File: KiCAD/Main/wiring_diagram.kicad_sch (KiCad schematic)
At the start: 20 parts, among them J5 Screw_Terminal_01x09, J6 Screw_Terminal_01x09, M1 Motor_Servo [Axon Mini MkII], M2 Motor_Servo [Axon Mini MkII], SW3 Screw Switch, SW4 Screw Switch, SW5 Screw Switch, SW6 Screw Switch

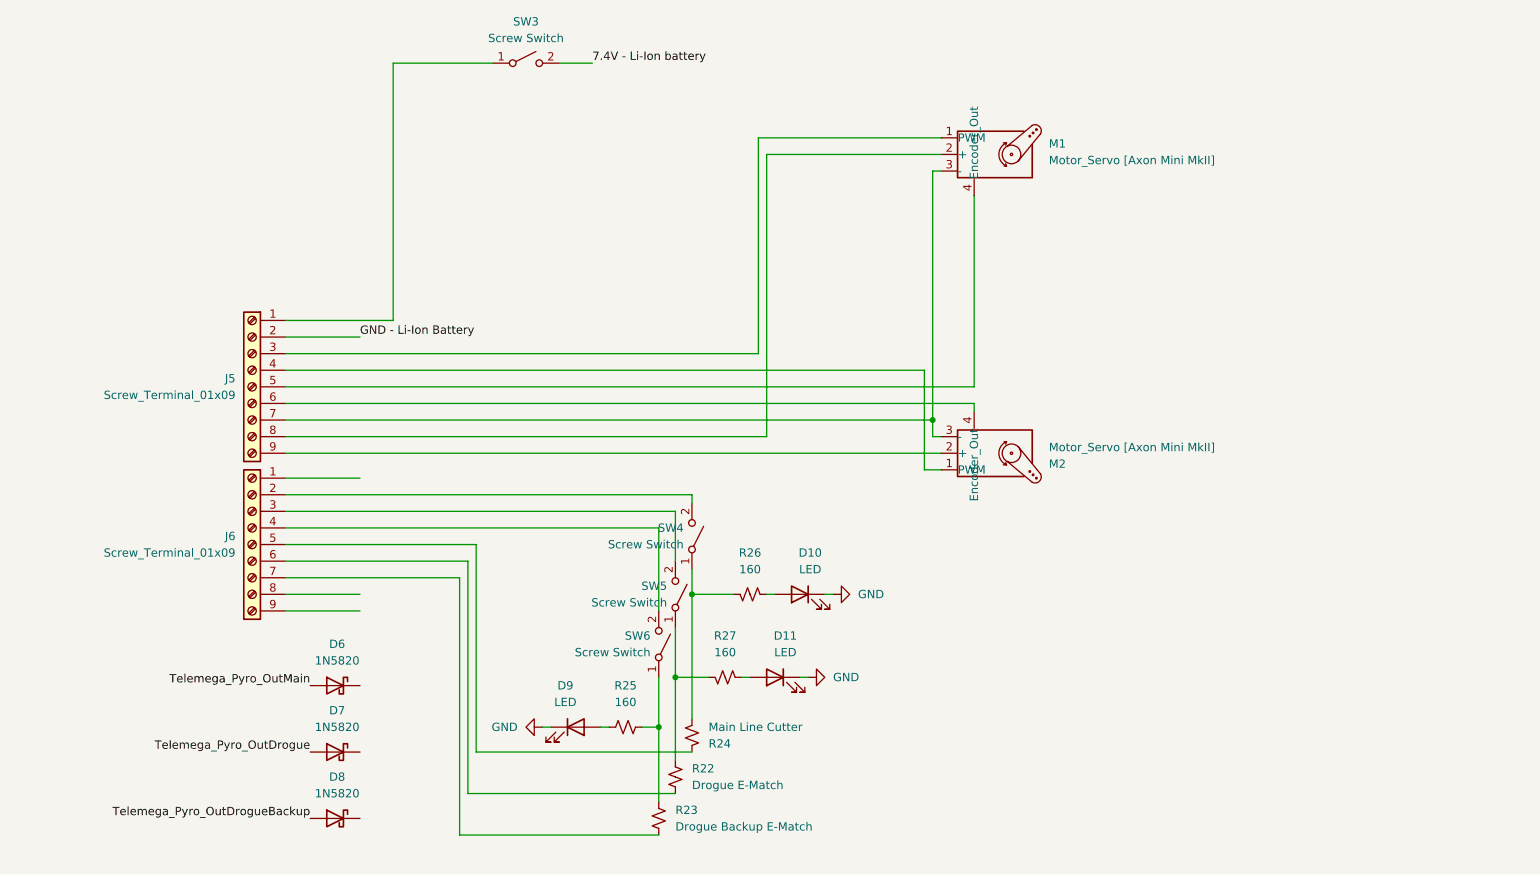
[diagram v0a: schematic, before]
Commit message: Update wiring diagram with TM input
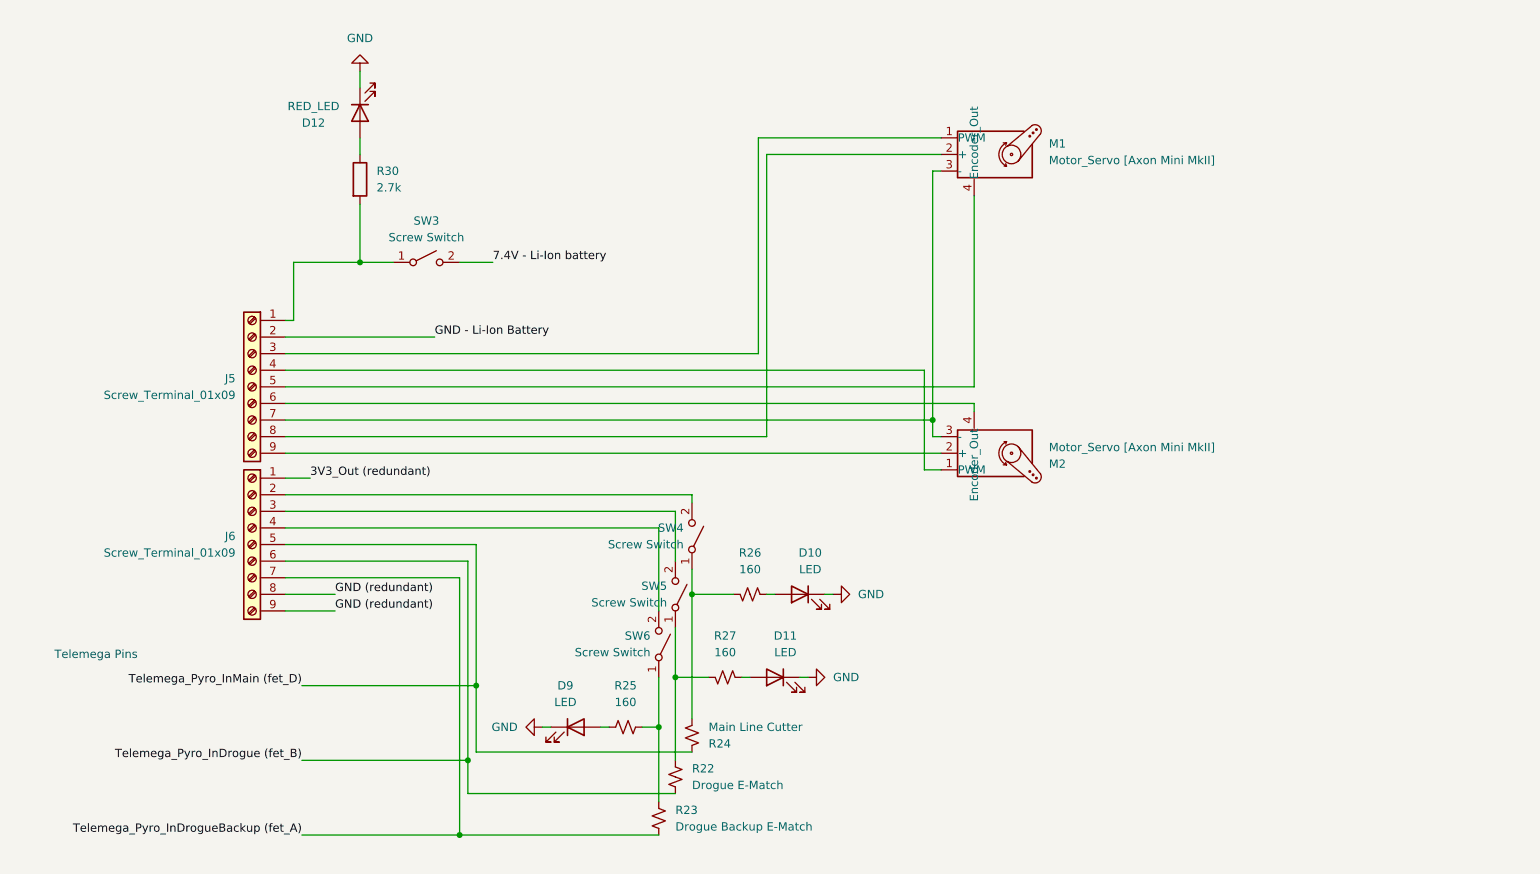
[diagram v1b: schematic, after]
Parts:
- removed D6, D7, D8: 1N5820, Diode_THT:D_DO-201AD_P15.24mm_Horizontal, symbol Diode:1N5820
- added D12: RED_LED, symbol Device:LED
- added R30: 2.7k, symbol Device:R
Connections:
- net GND: now also D12.1 (K)
- net Telemega_Pyro_InDrogue (fet_B): now reaches J6.6 (Drogue_Backup), R22.2
- net at J5.1 (7.4V_IN), SW3.1 (A): now also R30.2
- net Telemega_Pyro_InMain (fet_D): now reaches J6.5 (Drogue_Main), R24.1
- net 3V3_Out (redundant): now reaches J6.1 (3V3_OUT)
- net Telemega_Pyro_InDrogueBackup (fet_A): now reaches J6.7 (Main_Parachute), R23.2
- net GND (redundant): now reaches J6.8 (Pin_8)
- net GND (redundant): now also J6.9 (GND)
- new net: D12.2 (A), R30.1
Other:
- note added: "Telemega Pins"
- moved on the sheet: SW3

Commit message: Submit design for review
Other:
- moved on the sheet: D10, D11, M1, M2, R22, R24, R26, R27, SW4, SW5
